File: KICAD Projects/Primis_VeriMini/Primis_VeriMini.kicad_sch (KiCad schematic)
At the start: 28 parts, among them J1 USB-05, J2 Conn_ARM_SWD_TagConnect_TC203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, U1 nRF52833_QDxx, Y2 Crystal_GND24

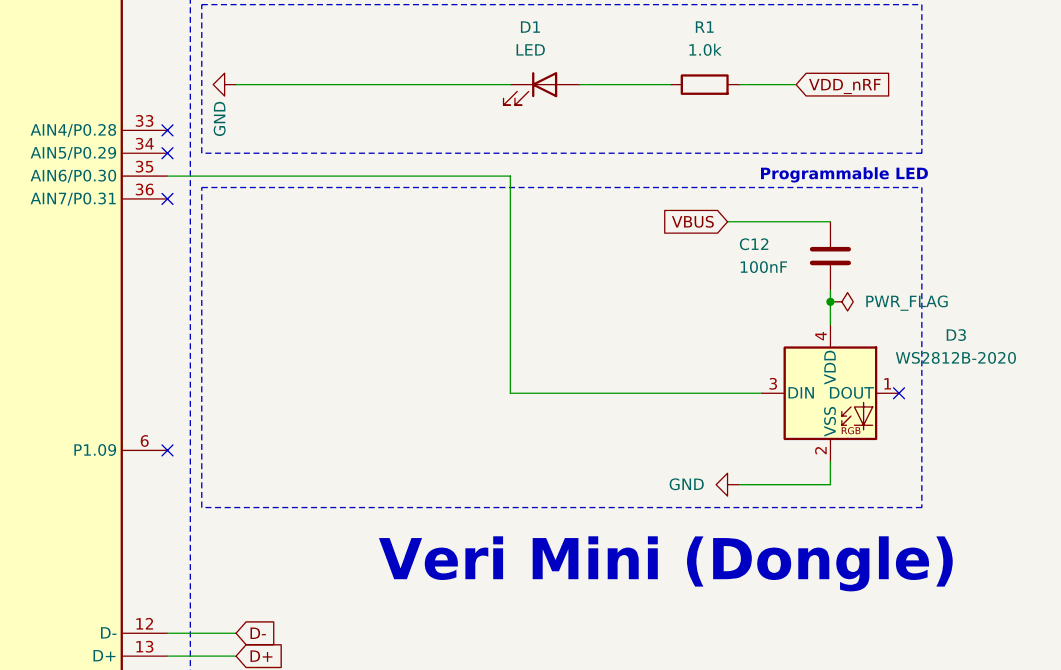
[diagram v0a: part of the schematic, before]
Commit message: Offical Frame CAD and more release
-Add a link to Valves Steam Frame repo
-Further iteration on Veri Mini
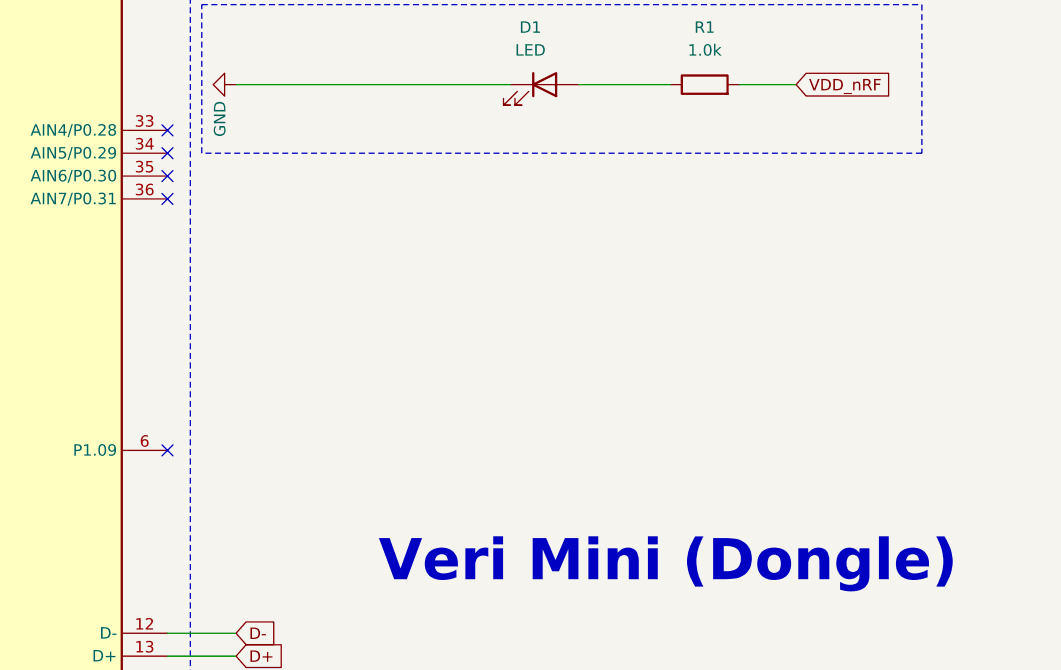
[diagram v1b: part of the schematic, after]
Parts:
- removed C12: 100nF, Capacitor_SMD:C_0402_1005Metric, symbol Device:C
- removed D3: WS2812B-2020, LED_SMD:LED_WS2812B-2020_PLCC4_2.0x2.0mm, symbol LED:WS2812B-2020
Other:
- note removed: "Programmable LED"
